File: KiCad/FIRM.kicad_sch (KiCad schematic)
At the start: 63 parts, among them J1 Conn_01x04_Pin, J3 Micro_SD_Card_Det2, J5 USB_C_Receptacle_USB2.0_16P, Q1 AO3401A, U1 STM32F405RGTx, U6 AP2112K-3.3, U7 W25Q128JVS, X2 32.768khz, Y1 12mhz

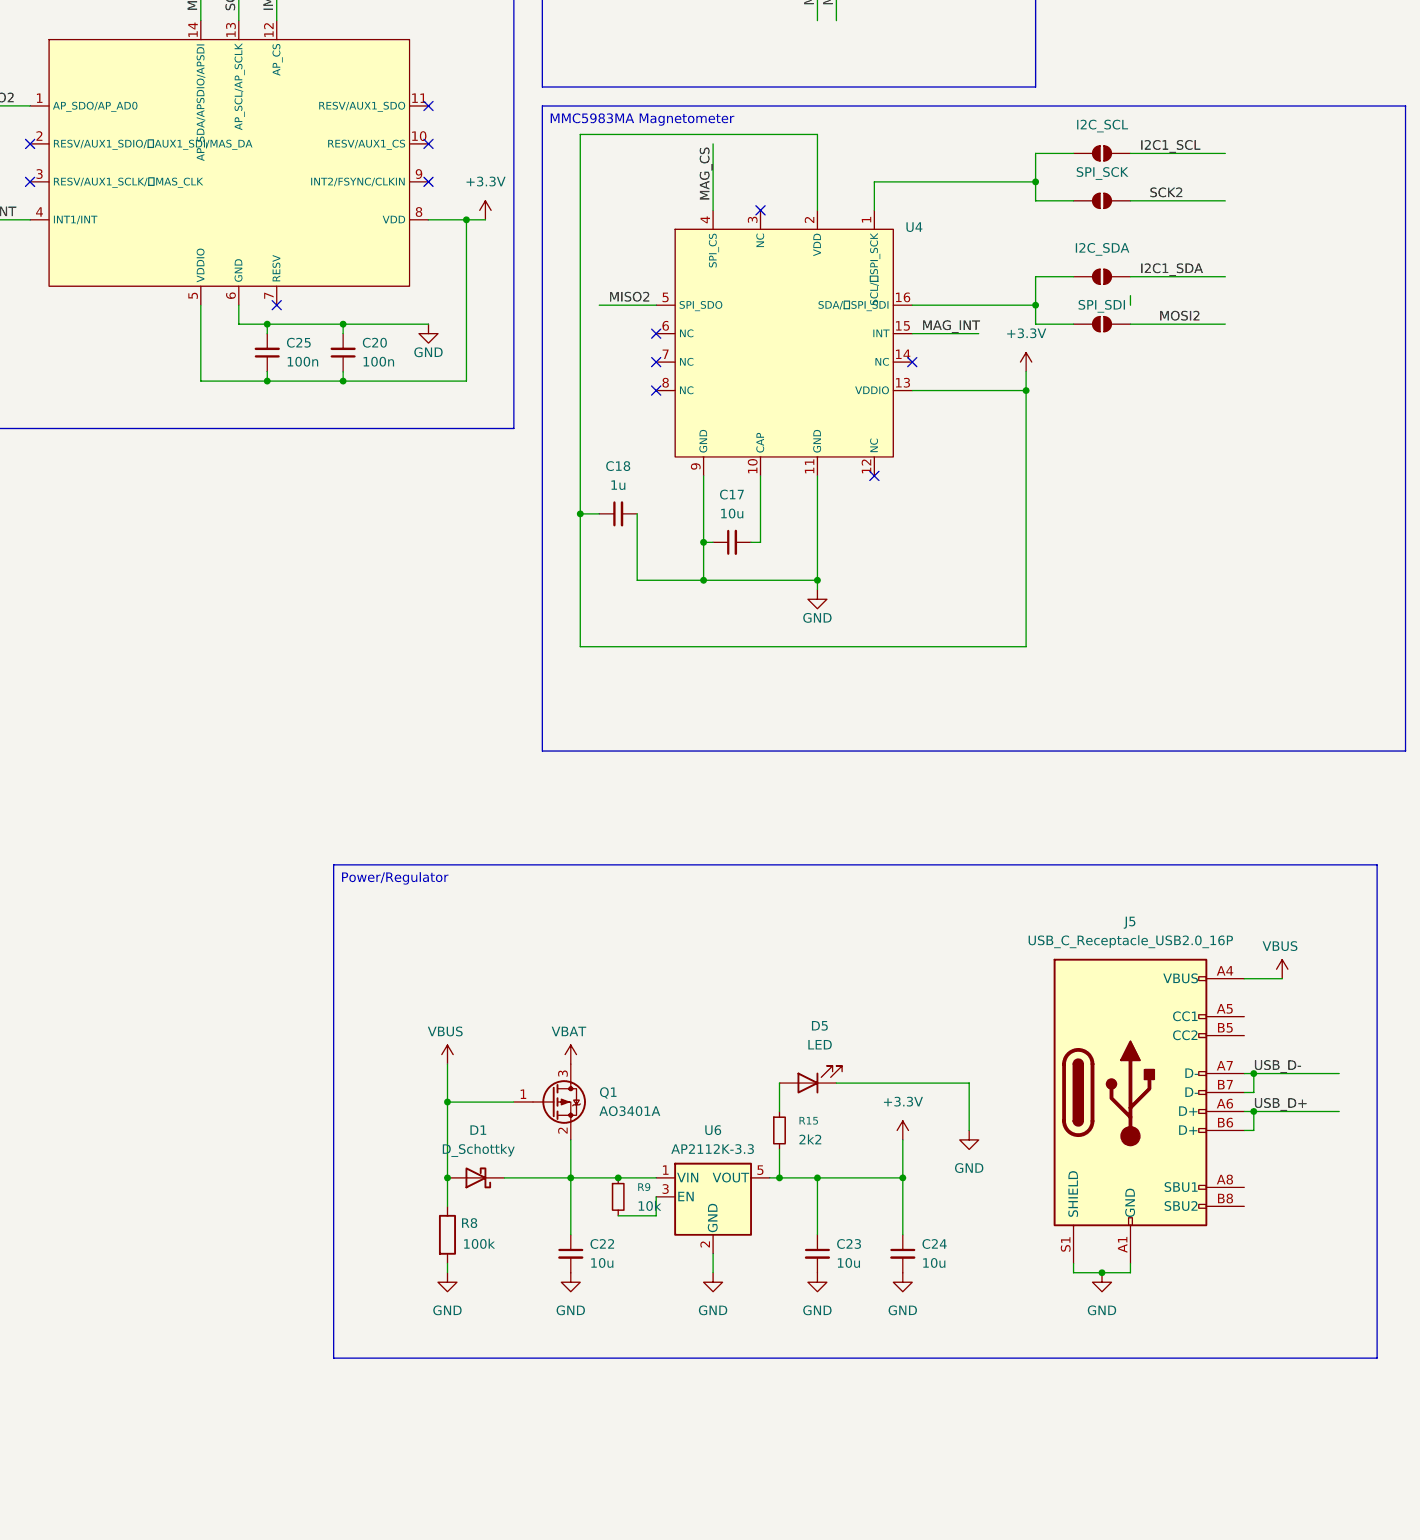
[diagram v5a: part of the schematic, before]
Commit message: USB-C pullup resistors and no-connects
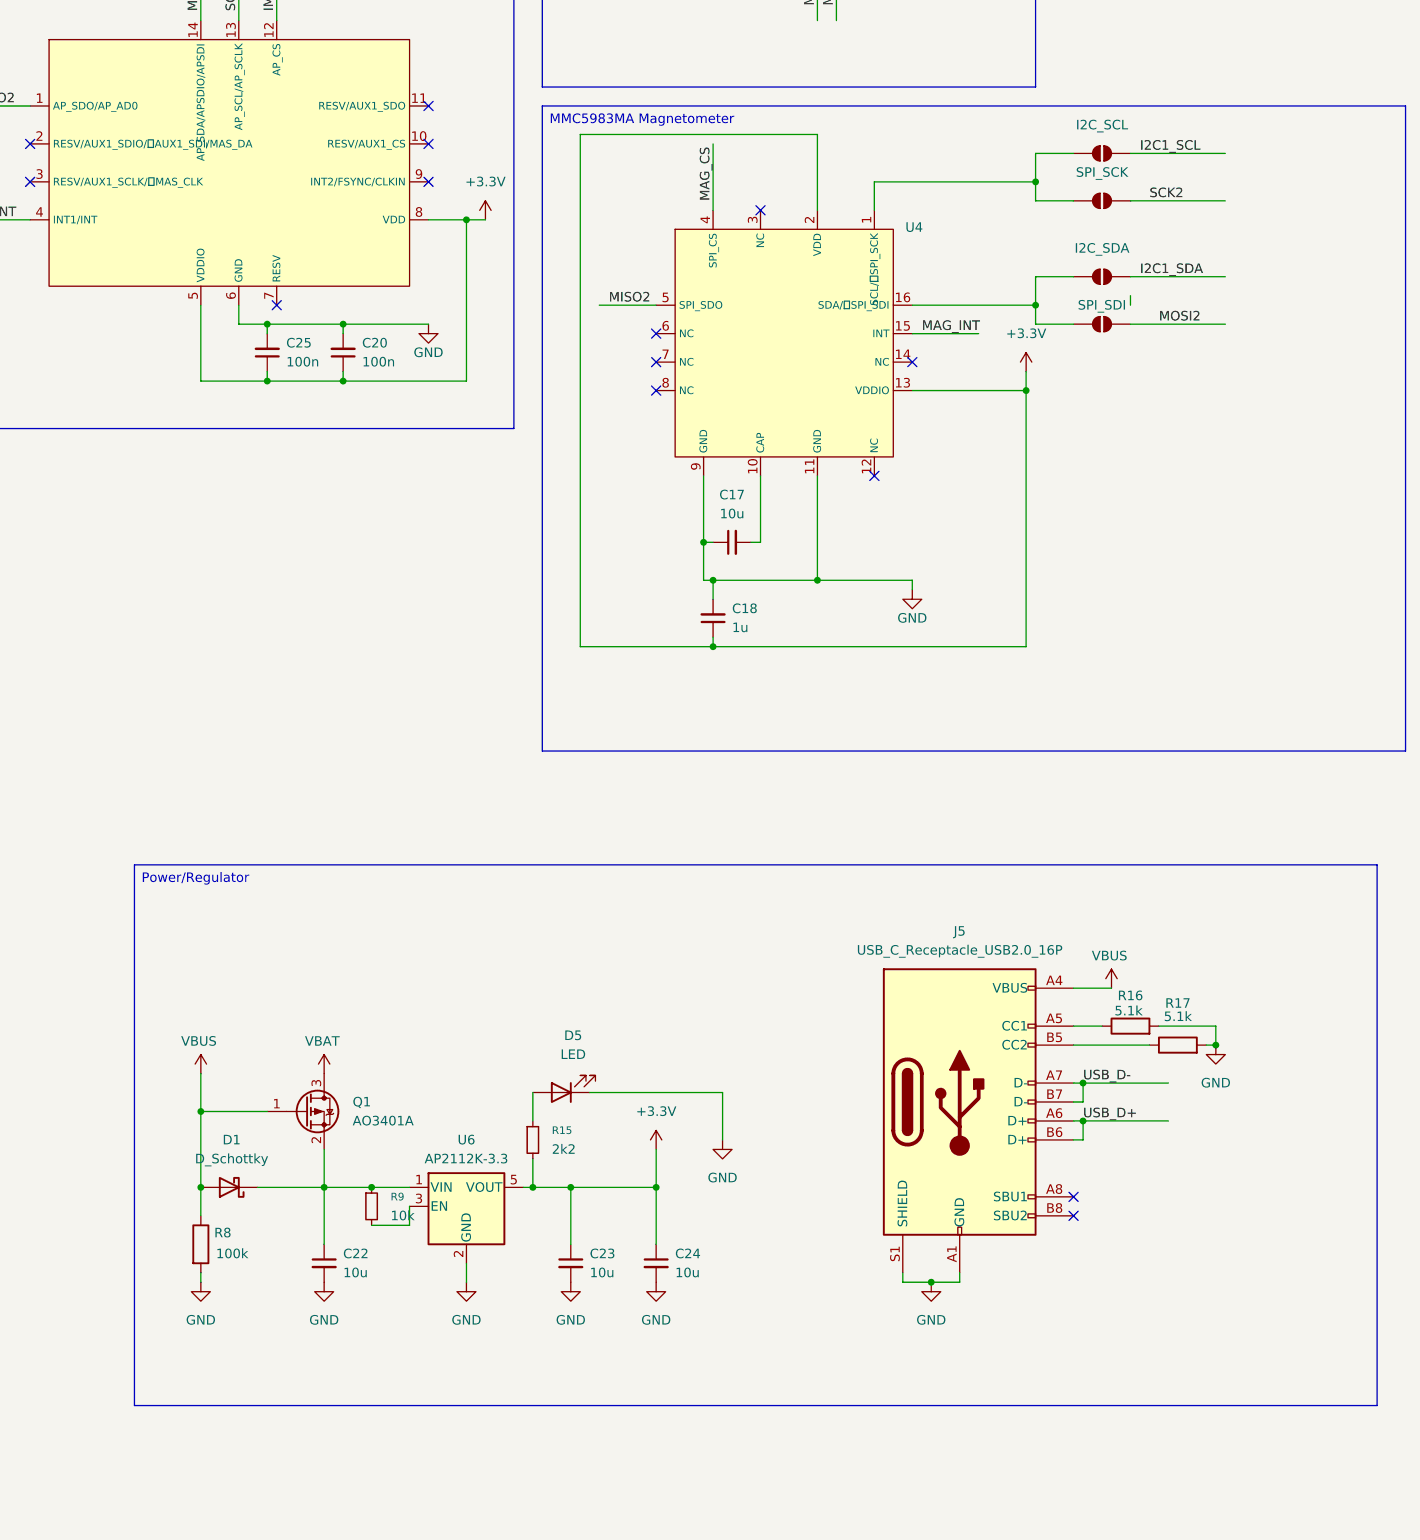
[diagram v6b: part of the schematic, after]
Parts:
- added R16, R17: 5.1k, symbol Device:R
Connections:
- net GND: now also R16.2, R17.2
- net at J5.A5 (CC1): now also R16.1
- net at J5.B5 (CC2): now also R17.1
- no-connect marks 12 -> 14
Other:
- moved on the sheet: C18, C22, C23, C24, D1, D5, J5, Q1, R15, R8, R9, U6

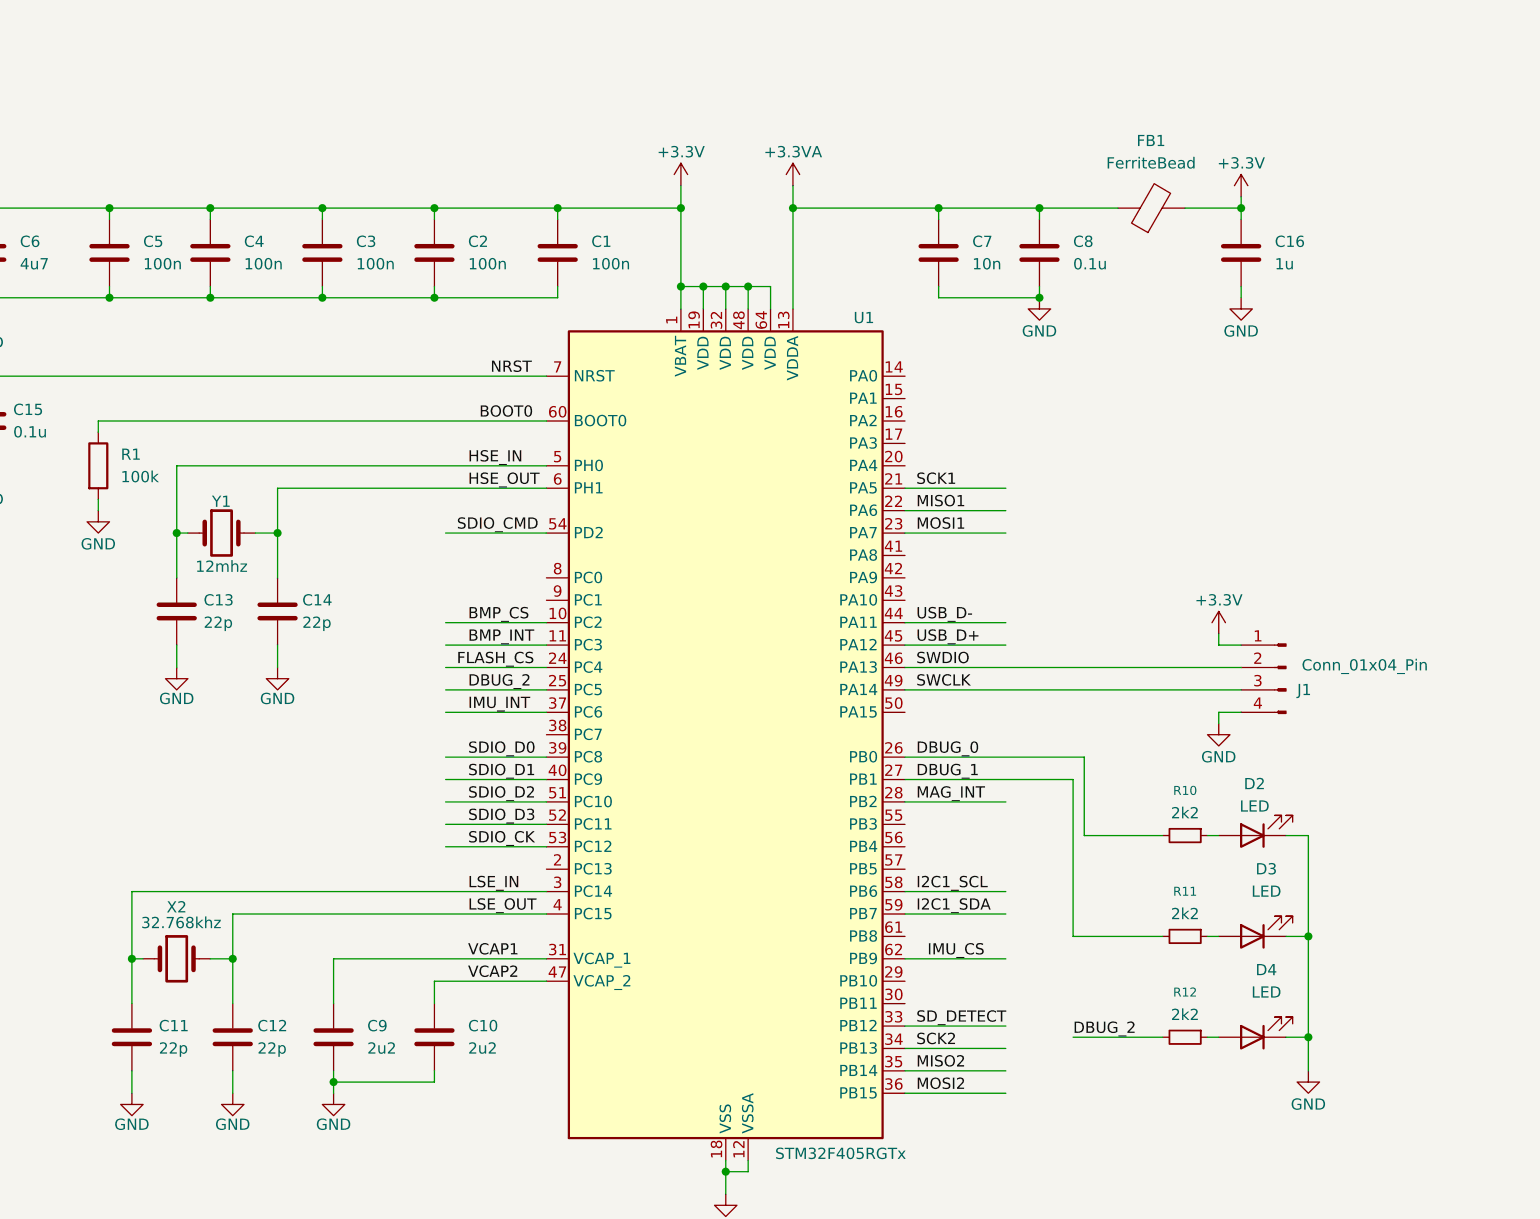
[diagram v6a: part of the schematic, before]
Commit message: add crystal parts
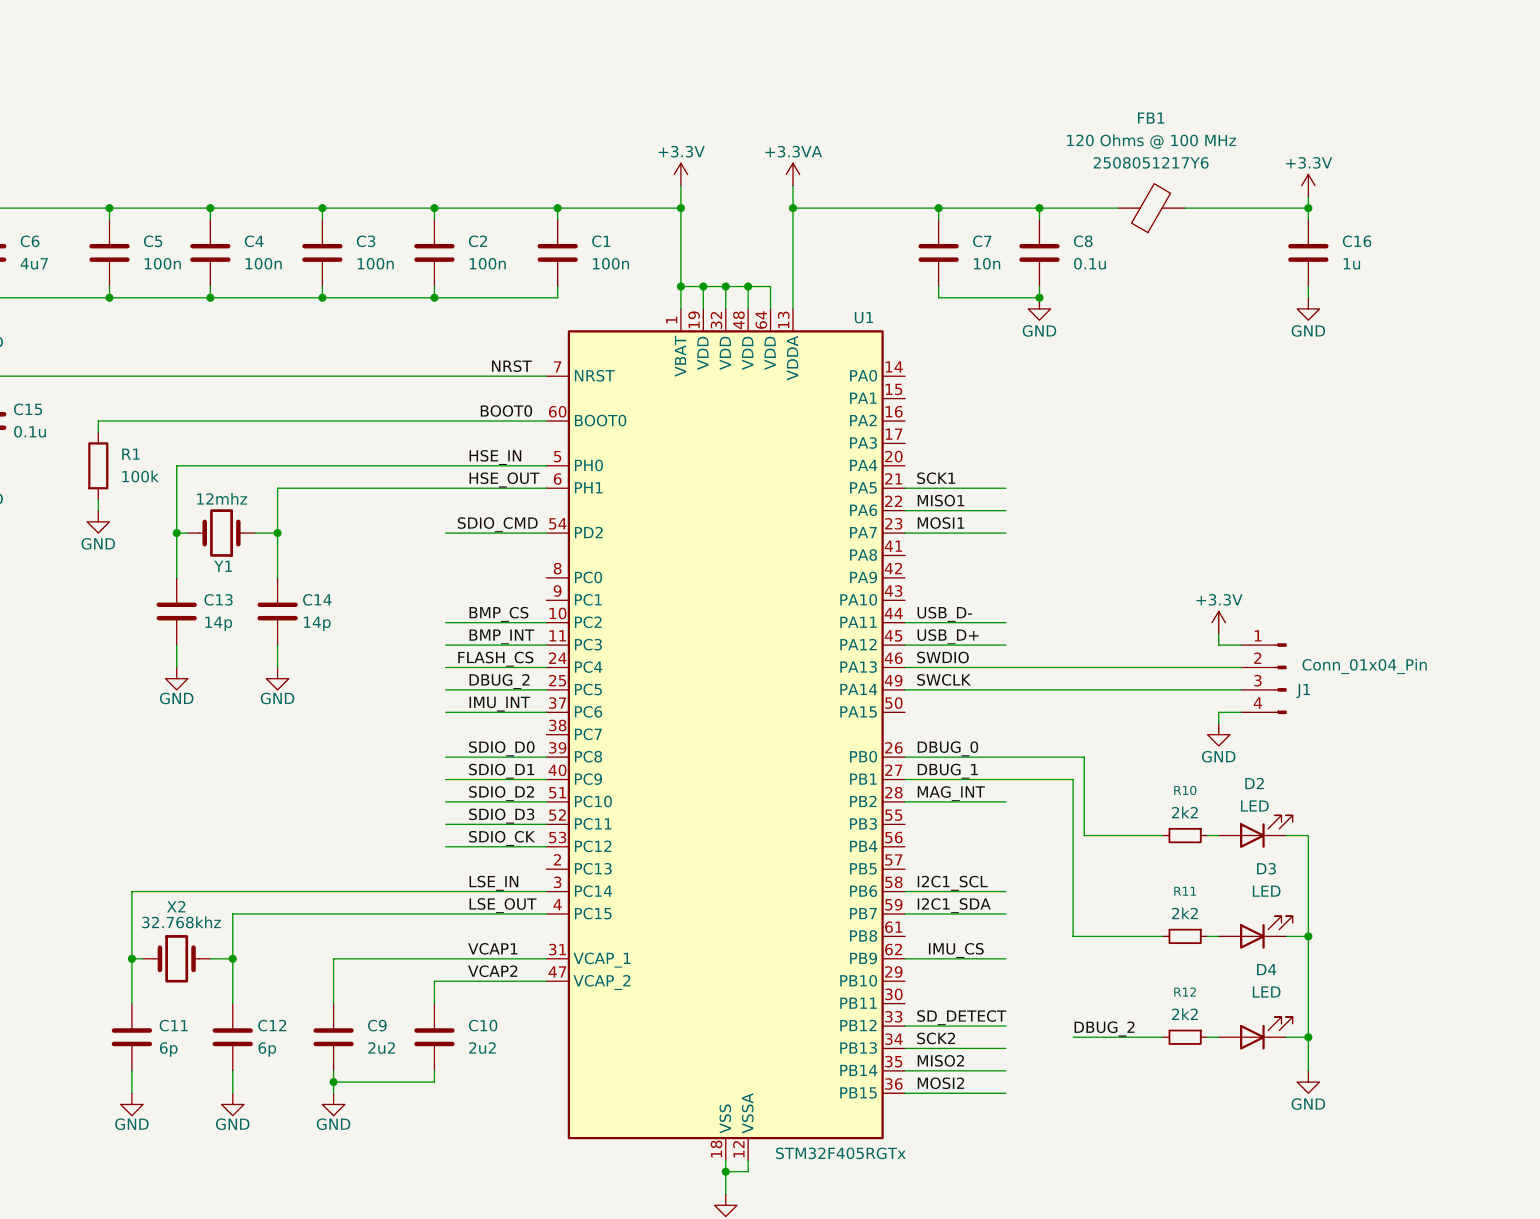
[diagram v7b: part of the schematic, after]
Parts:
- C11, C12: value 22p -> 6p
- C13, C14: value 22p -> 14p
- FB1: value FerriteBead -> 120 Ohms @ 100 MHz
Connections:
- net HSE_IN: now also Y1.2; no longer Y1.1
- net HSE_OUT: now also Y1.1; no longer Y1.2
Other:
- moved on the sheet: C16, Y1
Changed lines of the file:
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@@
 	)
 	(junction
-		(at 165.1 36.83)
+		(at 172.72 36.83)
 		(diameter 0)
 		(color 0 0 0 0)
@@
 	(wire
 		(pts
-			(xy 165.1 45.72) (xy 165.1 46.99)
+			(xy 172.72 45.72) (xy 172.72 46.99)
 		)
 		(stroke
@@
 	(wire
 		(pts
+			(xy 158.75 36.83) (xy 172.72 36.83)
+		)
+		(stroke
+			(width 0)
+			(type default)
+		)
+	)
+	(wire
+		(pts
 			(xy 40.64 185.42) (xy 40.64 189.23)
 		)
@@
 	(wire
 		(pts
-			(xy 158.75 36.83) (xy 165.1 36.83)
-		)
-		(stroke
-			(width 0)
-			(type default)
-		)
-	)
-	(wire
-		(pts
 			(xy 274.32 228.6) (xy 274.32 226.06)
 		)
@@
 	(wire
 		(pts
-			(xy 165.1 36.83) (xy 165.1 38.1)
+			(xy 172.72 36.83) (xy 172.72 38.1)
 		)
 		(stroke
@@
 	(wire
 		(pts
-			(xy 165.1 35.56) (xy 165.1 36.83)
+			(xy 172.72 35.56) (xy 172.72 36.83)
 		)
 		(stroke
@@
 	(symbol
 		(lib_id "Device:Crystal")
-		(at 49.53 73.66 0)
+		(at 49.53 73.66 180)
 		(unit 1)
 		(exclude_from_sim no)
@@
 		(dnp no)
 		(property "Reference" "Y1"
-			(at 49.53 70.104 0)
+			(at 49.784 77.47 0)
 			(effects
 				(font
@@
 		)
 		(property "Value" "12mhz"
-			(at 49.53 77.47 0)
+			(at 49.53 69.85 0)
 			(effects
 				(font
@@
 			)
 		)
-		(property "Datasheet" "~"
+		(property "Datasheet" "https://mm.digikey.com/Volume0/opasdata/d220001/medias/docus/6536/ABM8_Datasheet.pdf"
 			(at 49.53 73.66 0)
 			(effects
@@
 			)
 		)
-		(property "Description" "Two pin crystal"
+		(property "Description" "ABM8-272-T3"
 			(at 49.53 73.66 0)
 			(effects
@@
 	(symbol
 		(lib_id "power:GND")
-		(at 165.1 46.99 0)
+		(at 172.72 46.99 0)
 		(unit 1)
 		(exclude_from_sim no)
@@
 		(dnp no)
 		(property "Reference" "#PWR07"
-			(at 165.1 53.34 0)
+			(at 172.72 53.34 0)
 			(effects
 				(font
@@
 		)
 		(property "Value" "GND"
-			(at 165.1 50.8 0)
+			(at 172.72 50.8 0)
 			(effects
 				(font
@@
 		)
 		(property "Footprint" ""
-			(at 165.1 46.99 0)
+			(at 172.72 46.99 0)
 			(effects
 				(font
@@
 		)
 		(property "Datasheet" ""
-			(at 165.1 46.99 0)
+			(at 172.72 46.99 0)
 			(effects
 				(font
@@
 		)
 		(property "Description" "Power symbol creates a global label with name \"GND\" , ground"
-			(at 165.1 46.99 0)
+			(at 172.72 46.99 0)
 			(effects
 				(font
@@
 			)
 		)
-		(property "Value" "22p"
+		(property "Value" "14p"
 			(at 47.498 83.82 0)
 			(effects
@@
 			)
 		)
-		(property "Value" "22p"
+		(property "Value" "14p"
 			(at 58.674 83.82 0)
 			(effects
@@
 			)
 		)
-		(property "Value" "22p"
+		(property "Value" "6p"
 			(at 42.418 132.08 0)
 			(effects
@@
 	(symbol
 		(lib_id "Device:C")
-		(at 165.1 41.91 0)
+		(at 172.72 41.91 0)
 		(unit 1)
 		(exclude_from_sim no)
@@
 		(fields_autoplaced yes)
 		(property "Reference" "C16"
-			(at 168.91 40.6399 0)
+			(at 176.53 40.6399 0)
 			(effects
 				(font
@@
 		)
 		(property "Value" "1u"
-			(at 168.91 43.1799 0)
+			(at 176.53 43.1799 0)
 			(effects
 				(font
@@
 		)
 		(property "Footprint" ""
-			(at 166.0652 45.72 0)
+			(at 173.6852 45.72 0)
 			(effects
 				(font
@@
 		)
 		(property "Datasheet" "~"
-			(at 165.1 41.91 0)
+			(at 172.72 41.91 0)
 			(effects
 				(font
@@
 		)
 		(property "Description" "Unpolarized capacitor"
-			(at 165.1 41.91 0)
+			(at 172.72 41.91 0)
 			(effects
 				(font
@@
 			)
 		)
-		(property "Datasheet" "~"
+		(property "Datasheet" "https://ecsxtal.com/store/pdf/ECX_34R.pdf"
 			(at 44.45 121.92 0)
 			(effects
@@
 			)
 		)
-		(property "Description" "Two pin crystal"
+		(property "Description" "ECS-.327-6-34R-TR"
 			(at 44.45 121.92 0)
 			(effects
@@
 	(symbol
 		(lib_id "power:+3.3V")
-		(at 165.1 35.56 0)
+		(at 172.72 35.56 0)
 		(unit 1)
 		(exclude_from_sim no)
@@
 		(dnp no)
 		(property "Reference" "#PWR08"
-			(at 165.1 39.37 0)
+			(at 172.72 39.37 0)
 			(effects
 				(font
@@
 		)
 		(property "Value" "+3.3V"
-			(at 165.1 31.75 0)
+			(at 172.72 31.75 0)
 			(effects
 				(font
@@
 		)
 		(property "Footprint" ""
-			(at 165.1 35.56 0)
+			(at 172.72 35.56 0)
 			(effects
 				(font
@@
 		)
 		(property "Datasheet" ""
-			(at 165.1 35.56 0)
+			(at 172.72 35.56 0)
 			(effects
 				(font
@@
 		)
 		(property "Description" "Power symbol creates a global label with name \"+3.3V\""
-			(at 165.1 35.56 0)
+			(at 172.72 35.56 0)
 			(effects
 				(font
@@
 			)
 		)
-		(property "Value" "22p"
+		(property "Value" "6p"
 			(at 53.594 132.08 0)
 			(effects
@@
 		(on_board yes)
 		(dnp no)
-		(fields_autoplaced yes)
 		(property "Reference" "FB1"
-			(at 154.8892 29.21 90)
+			(at 154.8892 26.67 90)
 			(effects
 				(font
@@
 			)
 		)
-		(property "Value" "FerriteBead"
-			(at 154.8892 31.75 90)
+		(property "Value" "120 Ohms @ 100 MHz"
+			(at 154.8892 29.21 90)
 			(effects
 				(font
@@
 			)
 		)
-		(property "Datasheet" "~"
+		(property "Datasheet" "https://fair-rite.com/product/chip-beads-2508051217y6/"
 			(at 154.94 36.83 0)
 			(effects
@@
 			)
 		)
-		(property "Description" "Ferrite bead"
-			(at 154.94 36.83 0)
+		(property "Description" "2508051217Y6"
+			(at 154.8892 31.75 90)
 			(effects
 				(font
 					(size 1.27 1.27)
 				)
-				(hide yes)
 			)
 		)
